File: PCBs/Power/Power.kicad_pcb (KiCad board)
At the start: 2 copper layers, 50 x 50 mm, 9 parts, among them J2 Corner 1, J3 Corner 2, J4 Corner 3, J5 Corner 4, J6 Flight Controller

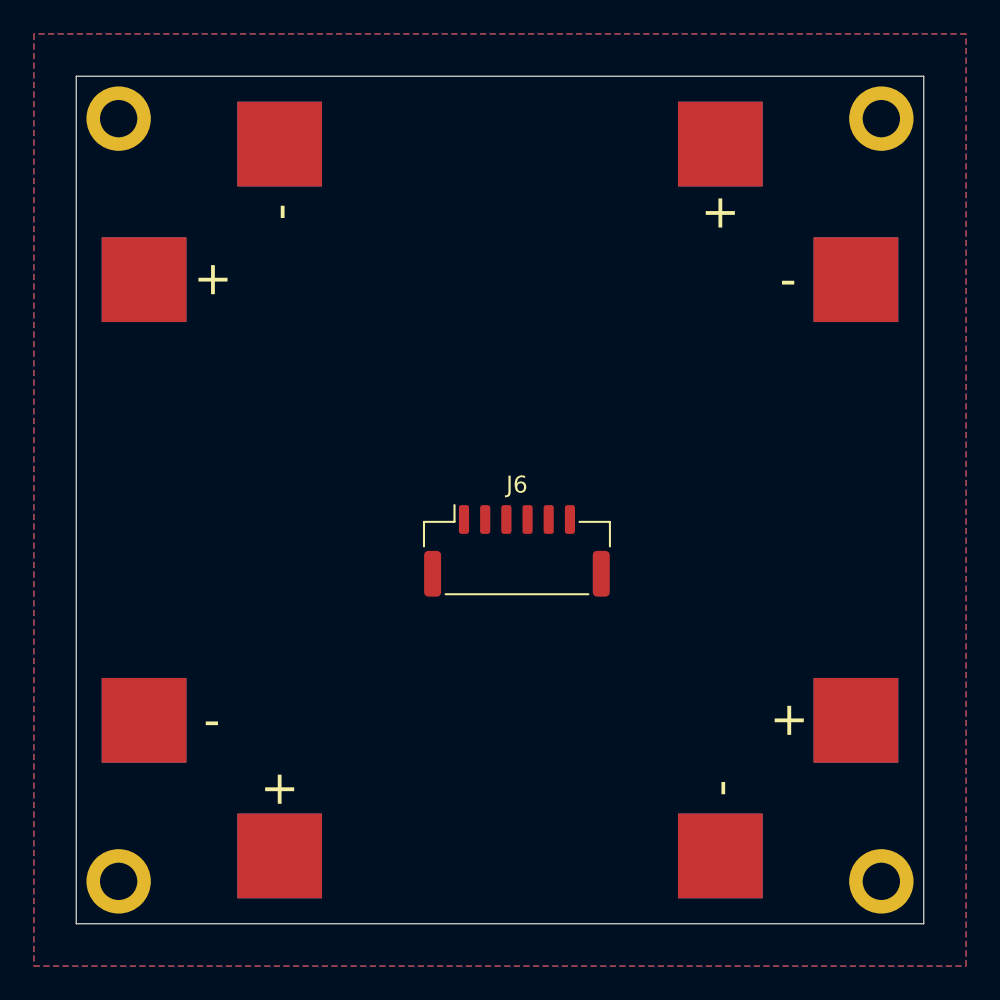
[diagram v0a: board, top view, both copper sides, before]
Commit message: all footprints complete
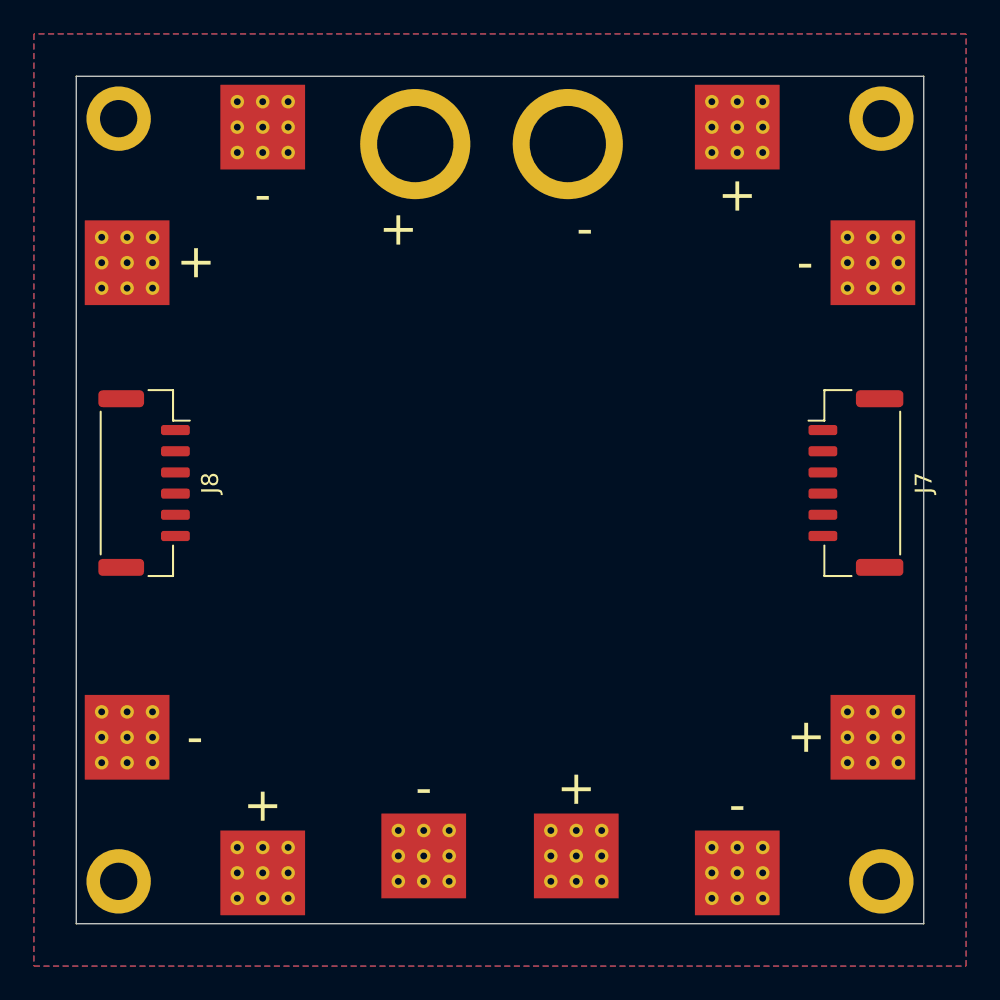
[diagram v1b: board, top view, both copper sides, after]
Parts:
- added J1: Power in SMD, Custom:SMD-Power, F.Cu at (175.0, 96.0)
- added J2: Power in THR, Custom:THR-Power, F.Cu at (174.5, 54.0)
- added J7: Flight Controller, Connector_JST:JST_GH_BM06B-GHS-TBT_1x06-1MP_P1.25mm_Vertical, F.Cu at (196.0, 74.0)
- moved J8 22.4 mm to (154.0, 74.0), turned to 270 degrees
- moved J3 1.41 mm to (157.0, 57.0)
- moved J4 1.41 mm to (193.0, 57.0)
- moved J5 1.41 mm to (193.0, 93.0)
- moved J6 1.41 mm to (157.0, 93.0)
- renumbered J2 to J3, J3 to J4, J4 to J5, J5 to J6, J6 to J8

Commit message: Board complete
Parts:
- moved J2 1.12 mm to (175.0, 55.0)
- moved J7 1.00 mm to (196.0, 75.0)
- moved J8 1.00 mm to (154.0, 75.0)
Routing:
- net VDD: track 0.00 -> 208.9 mm
- net GND: vias 0 -> 21
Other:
- board text added: "+"
- board text added: "-"
- board text added: "V1.0"
